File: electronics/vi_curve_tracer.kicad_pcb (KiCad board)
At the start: 2 copper layers, 27.9 x 38.1 mm, 29 parts, among them P1 CONN_01X05, P2 USB_OTG, P3 CONN_01X03, P4 CONN_01X03, U1 MCP6001, U2 pic24f08km202, U3 ft230x

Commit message: Added electronics files, nearly complete
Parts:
- added C12: 100nF, kicad_pcb:SM_0603, F.Cu at (208.3, 91.9)
- added C13: 100nF, kicad_pcb:SM_0603, F.Cu at (208.3, 98.0)
- added C14: 100nF, kicad_pcb:SM_0603, F.Cu at (211.1, 91.9)
- added C15: 1uF, kicad_pcb:SM_0603, F.Cu at (180.1, 97.8)
- added C16: 1uF, kicad_pcb:SM_0603, F.Cu at (212.3, 86.1)
- added C17: 1uF, kicad_pcb:SM_0603, F.Cu at (212.3, 87.6)
- added C18: 1uF, kicad_pcb:SM_0603, F.Cu at (212.3, 101.3)
- added C19: 1uF, kicad_pcb:SM_0603, F.Cu at (183.1, 78.7)
- added C20: 1uF, kicad_pcb:SM_0603, F.Cu at (184.7, 78.7)
- added C21: 1uF, kicad_pcb:SM_0603, F.Cu at (186.2, 78.7)
- added C22: 1uF, kicad_pcb:SM_0603, F.Cu at (174.2, 91.9)
- added C8: 100nF, kicad_pcb:SM_0603, F.Cu at (211.1, 98.0)
- added R13: 1k, kicad_pcb:SM_0603, F.Cu at (208.3, 96.5)
- added R14: 1k, kicad_pcb:SM_0603, F.Cu at (211.1, 90.4)
- added R15: 1k, kicad_pcb:SM_0603, F.Cu at (180.1, 96.3)
- added REF**: case_sickOfBeige_60x37, kicad_pcb:case_sickOfBeige_60x37, F.Cu at (196.5, 91.5)
- added W1: TEST_1P, Measurement_Points:Measurement_Point_Round-SMD-Pad_Small, F.Cu at (174.2, 94.7)
- added W10: TEST_1P, Measurement_Points:Measurement_Point_Round-SMD-Pad_Small, F.Cu at (193.3, 100.8)
- added W2: TEST_1P, Measurement_Points:Measurement_Point_Round-SMD-Pad_Small, F.Cu at (174.2, 87.5)
- added W3: TEST_1P, Measurement_Points:Measurement_Point_Round-SMD-Pad_Small, F.Cu at (174.2, 89.5)
- added W4: TEST_1P, Measurement_Points:Measurement_Point_Round-SMD-Pad_Small, F.Cu at (174.2, 85.5)
- added W5: TEST_1P, Measurement_Points:Measurement_Point_Round-SMD-Pad_Small, F.Cu at (187.8, 95.2)
- added W6: TEST_1P, Measurement_Points:Measurement_Point_Round-SMD-Pad_Small, F.Cu at (185.8, 97.3)
- added W7: TEST_1P, Measurement_Points:Measurement_Point_Round-SMD-Pad_Small, F.Cu at (185.8, 95.2)
- added W8: TEST_1P, Measurement_Points:Measurement_Point_Round-SMD-Pad_Small, F.Cu at (187.8, 97.3)
- added W9: TEST_1P, Measurement_Points:Measurement_Point_Round-SMD-Pad_Small, F.Cu at (191.3, 100.8)
- P2: moved to F.Cu
- R12: value 100 -> 10
- R2, R3: value 10k -> 100k
- R6, R7, R8: value 100 -> 1k
- U1: value MCP6001 -> MCP6004; footprint kicad_pcb:SOT-23-5 -> SMD_Packages:SSOP-14
- moved C3 80.6 mm to (210.1, 84.1), turned to 0 degrees
- moved P2 77.6 mm to (209.8, 73.2), turned to 180 degrees
- moved R9 76.2 mm to (207.1, 82.5), turned to 0 degrees
- moved R10 74.7 mm to (207.1, 81.0), turned to 0 degrees
- moved C5 73.2 mm to (207.1, 79.5), turned to 180 degrees
- moved C9 72.3 mm to (201.4, 90.9)
- moved U1 70.9 mm to (201.4, 94.5), turned to 270 degrees
- moved U3 69.2 mm to (199.3, 80.8)
- moved C1 68.5 mm to (212.1, 79.5)
- moved R11 68.2 mm to (208.3, 90.4), turned to 0 degrees
- moved R8 67.7 mm to (211.1, 96.5)
- moved R4 67.0 mm to (201.4, 98.0)
- moved R2 66.0 mm to (194.3, 97.5), turned to 180 degrees
- moved R5 63.8 mm to (198.6, 98.0), turned to 0 degrees
- moved R3 60.1 mm to (194.3, 96.0)
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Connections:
- C2 pad 1: HZ_OUT_0 -> Net-(C2-Pad1)
- C4 pad 1: HZ_OUT_1 -> Net-(C4-Pad1)
- C6 pad 1: HZ_OUT_2 -> Net-(C6-Pad1)
- P1 pad 1: +5V -> ~MCLR
- P1 pad 2: ~MCLR -> +5V
- P3 pad 1: HZ_OUT_2 -> /GateVoltage
- P4 pad 1: HZ_OUT_2 -> /GateVoltage
- R11 pad 1: LD_VOLTAGE_0 -> Net-(C12-Pad1)
- R11 pad 2: LZ_OUT_0 -> Net-(C14-Pad1)
- R12 pad 1: LZ_OUT_1 -> /-Vout
- R3 pad 2: HZ_OUT_0 -> /IsenseReference
- R5 pad 1: LZ_OUT_1 -> /-Vout
- R6 pad 1: HZ_OUT_2 -> Net-(C6-Pad1)
- R7 pad 1: HZ_OUT_1 -> Net-(C4-Pad1)
- R8 pad 1: HZ_OUT_0 -> Net-(C8-Pad1)
- R8 pad 2: Net-(R8-Pad2) -> /DAC_high
- U1 pad 1: Net-(R2-Pad1) -> /IsenseReference
- U1 pad 2: GNDD -> /IsenseReference
- U1 pad 3: Net-(R3-Pad1) -> Net-(C4-Pad1)
- U1 pad 4: Net-(R2-Pad2) -> +5V
- U1 pad 5: +5V -> Net-(R3-Pad1)
- U2 pad 10: HZ_OUT_0 -> Net-(U2-Pad10)
- U2 pad 11: HZ_OUT_1 -> Net-(U2-Pad11)
- U2 pad 12: HZ_OUT_2 -> (no net)
- U2 pad 17: (no net) -> Net-(R2-Pad1)
- U2 pad 18: (no net) -> Net-(U2-Pad18)
- U2 pad 19: (no net) -> Net-(U2-Pad19)
- U2 pad 20: Net-(R8-Pad2) -> Net-(C2-Pad1)
- U2 pad 23: LZ_OUT_0 -> /DAC_low
- U2 pad 25: LZ_OUT_1 -> /DAC_high
- U2 pad 7: Net-(R2-Pad1) -> (no net)
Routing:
- net GNDD: track 27.9 -> 79.1 mm, vias 11 -> 19
- net HZ_OUT_2: track 42.5 -> 0.00 mm, vias 2 -> 0
- net /DAC_high: track 0.00 -> 38.0 mm
- net LZ_OUT_1: track 30.5 -> 0.00 mm, vias 2 -> 0
- net /GateVoltage: track 0.00 -> 29.5 mm
- net /DAC_low: track 0.00 -> 28.0 mm
- net HZ_OUT_0: track 26.2 -> 0.00 mm, vias 3 -> 0
- net /-Vout: track 0.00 -> 23.9 mm, vias 0 -> 4
- net +5V: track 18.1 -> 41.9 mm, vias 1 -> 11
- net FT230X_RX: track 11.6 -> 30.5 mm
- net /IsenseReference: track 0.00 -> 17.3 mm, vias 0 -> 2
- net HZ_OUT_1: track 16.1 -> 0.00 mm, vias 2 -> 0
- net LD_VOLTAGE_0: track 48.3 -> 62.4 mm
- net FT230X_TX: track 16.2 -> 28.9 mm
- net Net-(R3-Pad1): track 4.15 -> 16.9 mm
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- added copper zone on B.Cu, net +5V
- removed copper zone on F.Cu, net +5V
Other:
- board size 27.9 x 38.1 mm -> 60 x 37 mm

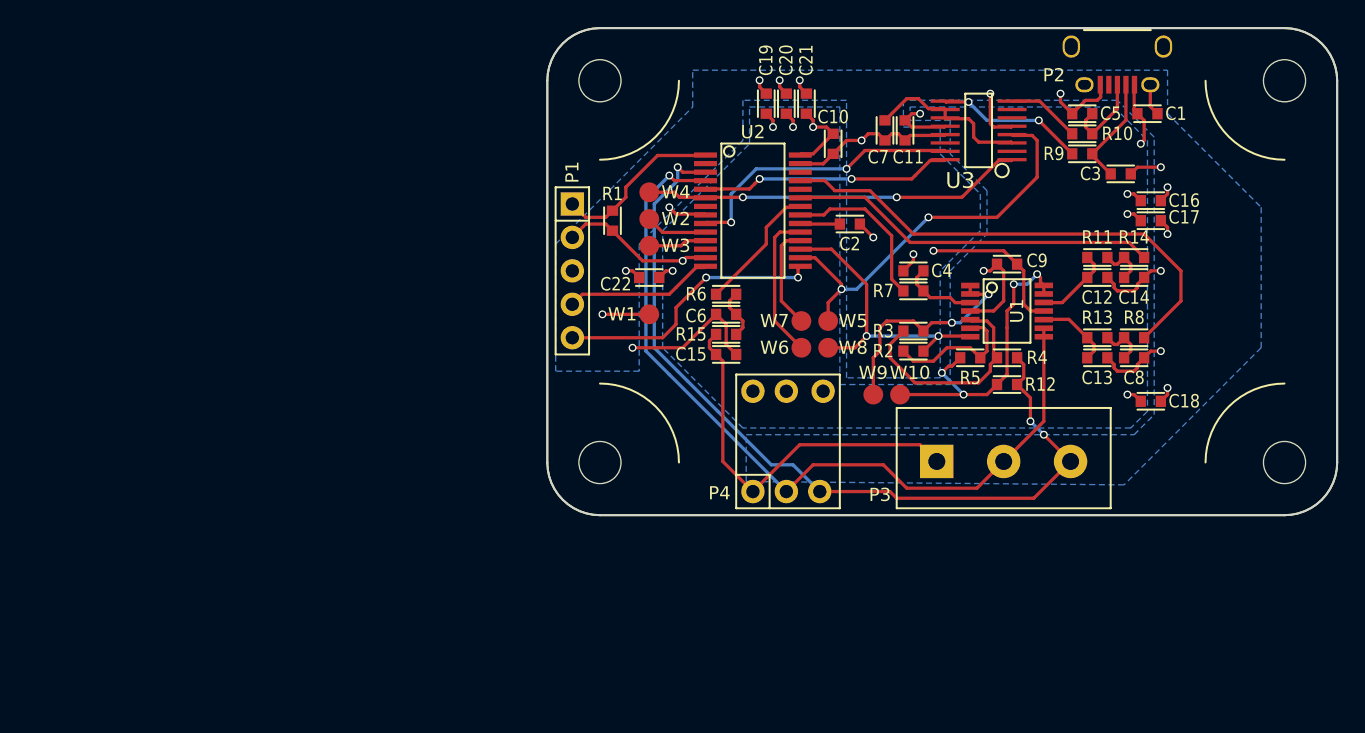
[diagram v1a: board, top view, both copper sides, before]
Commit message: Updated electronics with most recent layout and schematic
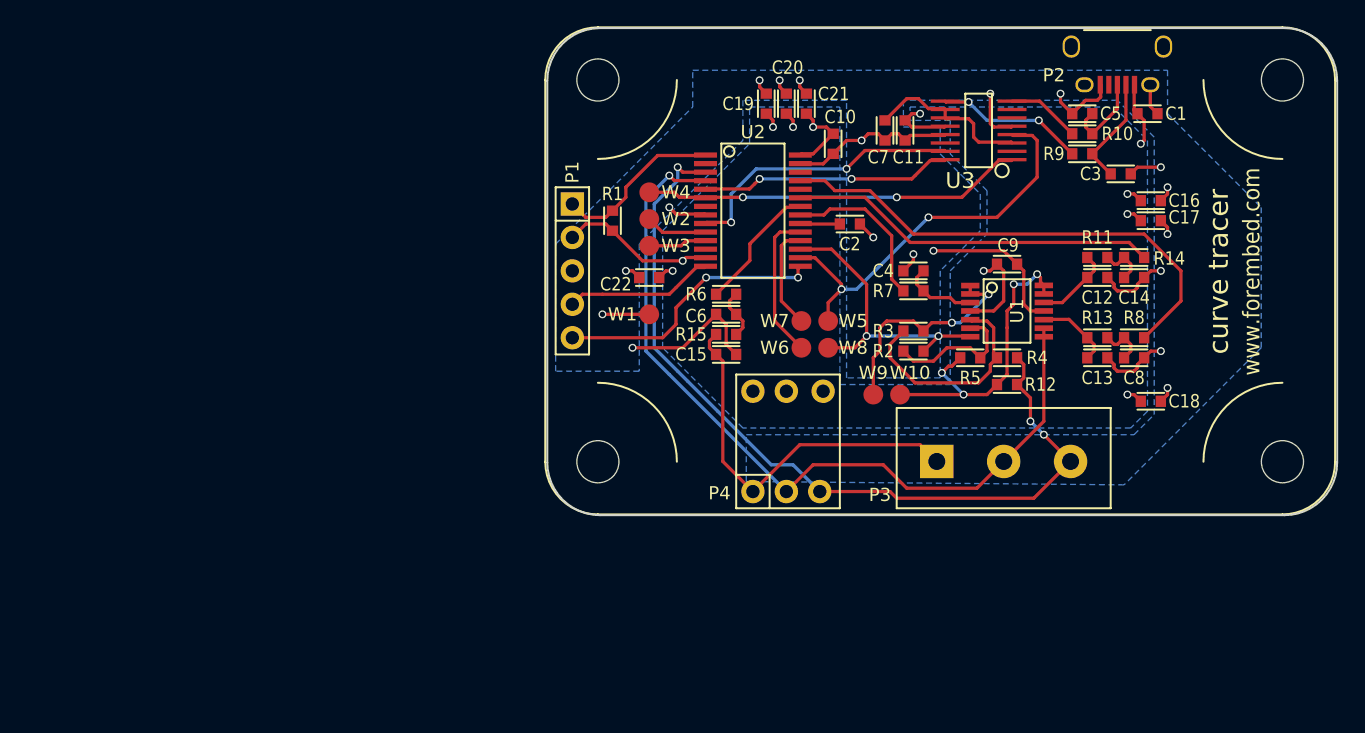
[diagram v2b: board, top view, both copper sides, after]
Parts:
- moved REF** 0.17 mm to (196.3, 91.4)
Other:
- board text added: "curve tracer"
- board text added: "www.forembed.com"

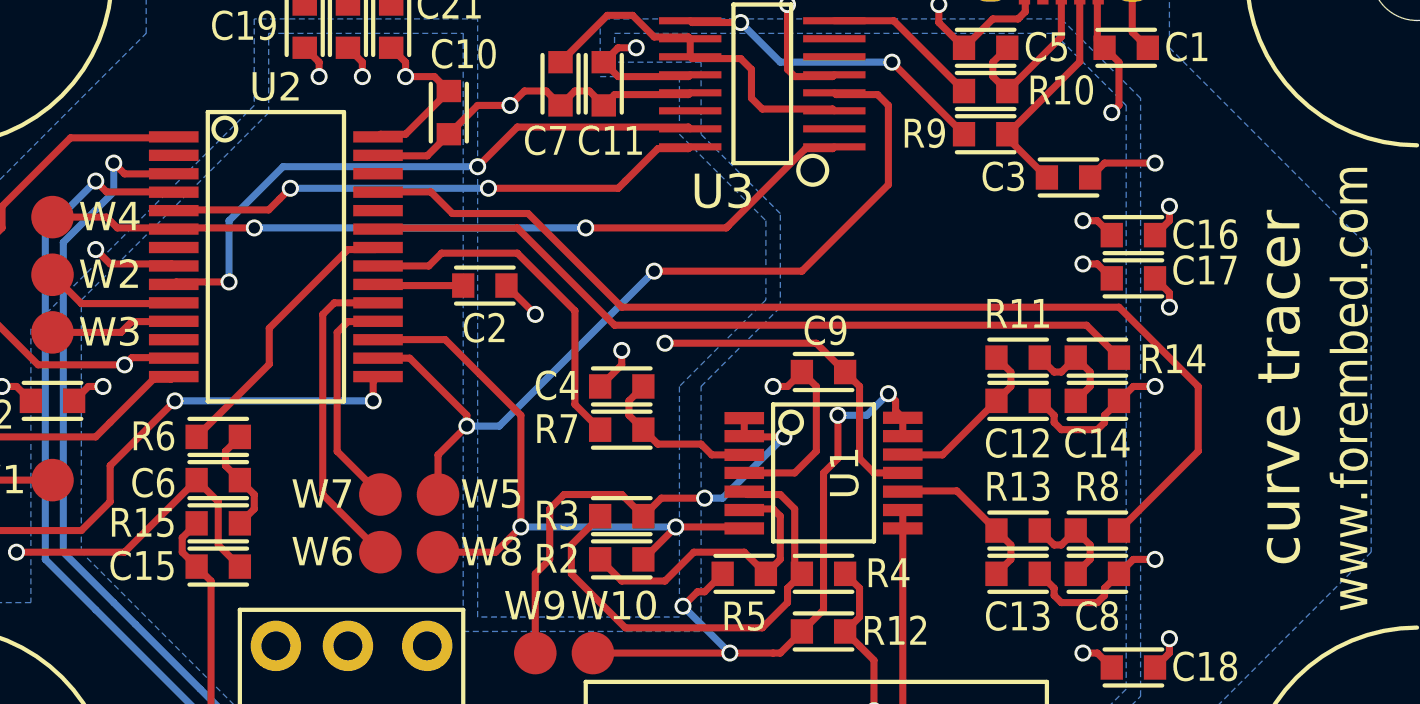
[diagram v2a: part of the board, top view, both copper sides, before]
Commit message: #4 Port complete for C code, had to move DAC outputs to opamp outputs on board to improve impedance
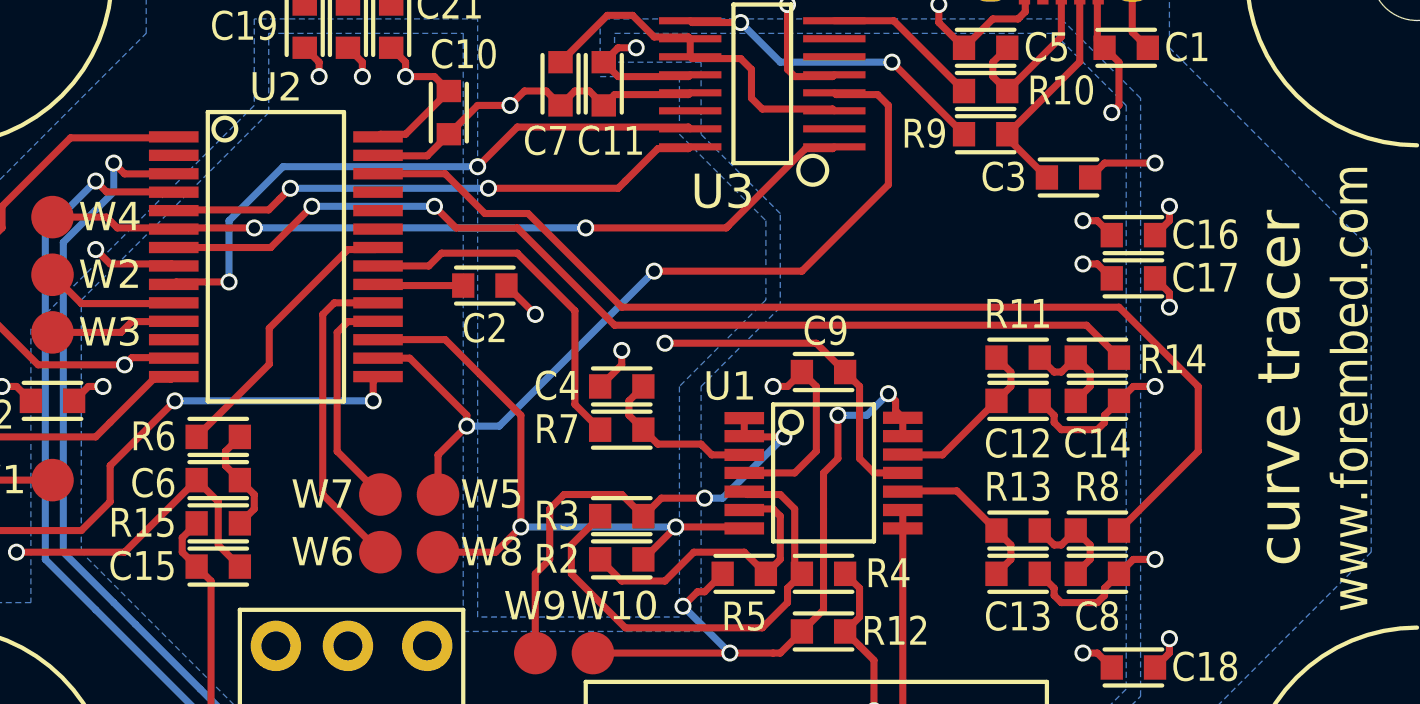
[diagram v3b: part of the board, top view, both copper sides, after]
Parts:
- R1: value 1k -> 10k
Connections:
- net Net-(R6-Pad2) renamed /PWM2
- net Net-(R7-Pad2) renamed /PWM1
- U2 pad 23: /DAC_low -> (no net)
- U2 pad 25: /DAC_high -> (no net)
- U2 pad 26: (no net) -> /DAC_high
- U2 pad 7: (no net) -> /DAC_low
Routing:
- net /DAC_low: track 28.0 -> 36.2 mm, vias 0 -> 2

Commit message: Minor rev of electronics, added BOM
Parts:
- added C23: 1uF, kicad_pcb:SM_0603, F.Cu at (191.4, 91.4)
- added R16: 10k, kicad_pcb:SM_0603, F.Cu at (191.4, 93.0)
- R2, R3: value 100k -> 10k
- R7: value 1k -> 10k
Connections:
- R7 pad 2: /PWM1 -> Net-(C23-Pad1)
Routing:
- net Net-(C23-Pad1): track 0.00 -> 3.76 mm
- net GNDD: track 79.1 -> 81.9 mm
- net /PWM1: track 12.5 -> 10.5 mm
- net Net-(R2-Pad1): track 22.9 -> 22.3 mm
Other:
- board text added: "curve tracer v1.0"
- board text removed: "curve tracer"

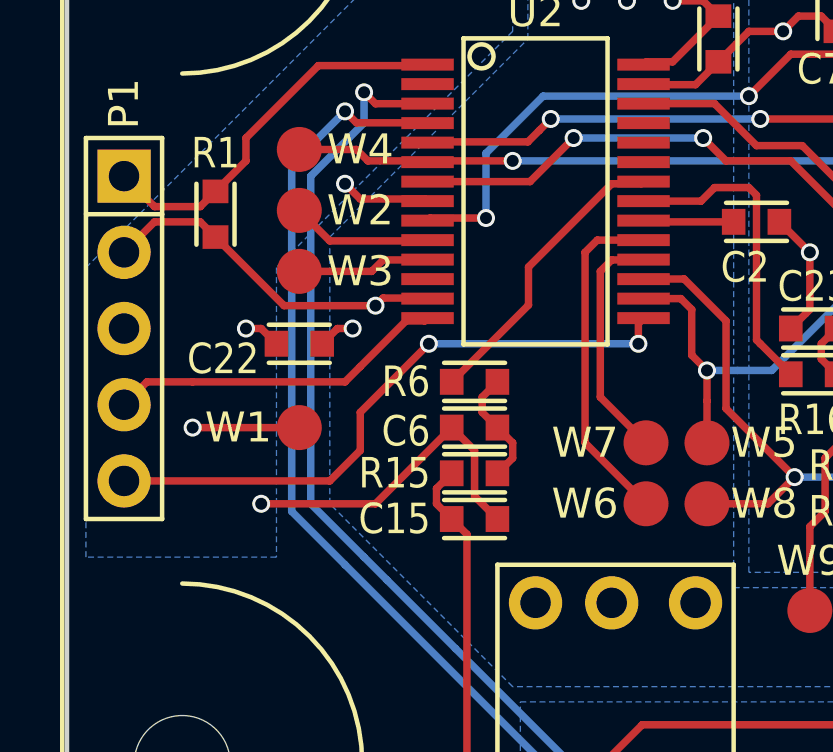
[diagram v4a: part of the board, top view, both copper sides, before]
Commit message: See #5 - Added patch wire to control the gate voltage
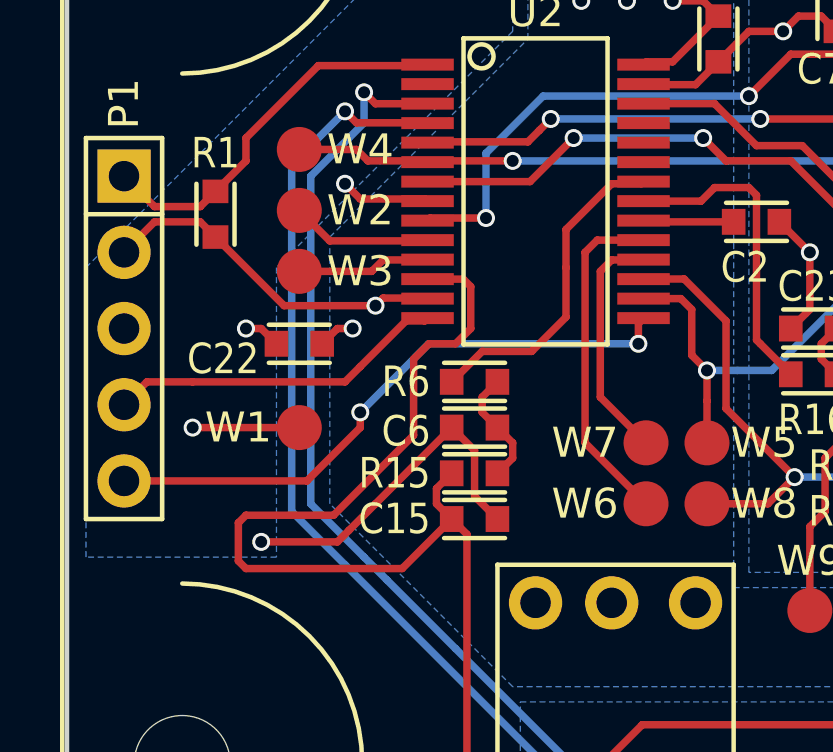
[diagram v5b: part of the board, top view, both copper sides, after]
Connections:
- C15 pad 1: /GateVoltage -> GateVoltage
- P3 pad 1: /GateVoltage -> GateVoltage
- P4 pad 1: /GateVoltage -> GateVoltage
- R15 pad 1: /GateVoltage -> GateVoltage
- U2 pad 12: (no net) -> GateVoltage
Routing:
- net GateVoltage: track 0.00 -> 53.5 mm
- net /GateVoltage: track 29.5 -> 0.00 mm
- net /PWM2: track 9.98 -> 10.9 mm
- net GNDD: track 81.9 -> 82.4 mm
